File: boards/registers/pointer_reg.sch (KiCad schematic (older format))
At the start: 48 parts, among them U10 74HC161PW, U11 MC74HC244ADT, U12 MC74HC244ADT, U13 74HC161PW, U14 74HC161PW, U15 MC74HC244ADT, U16 MC74HC244ADT, U9 74HC161PW

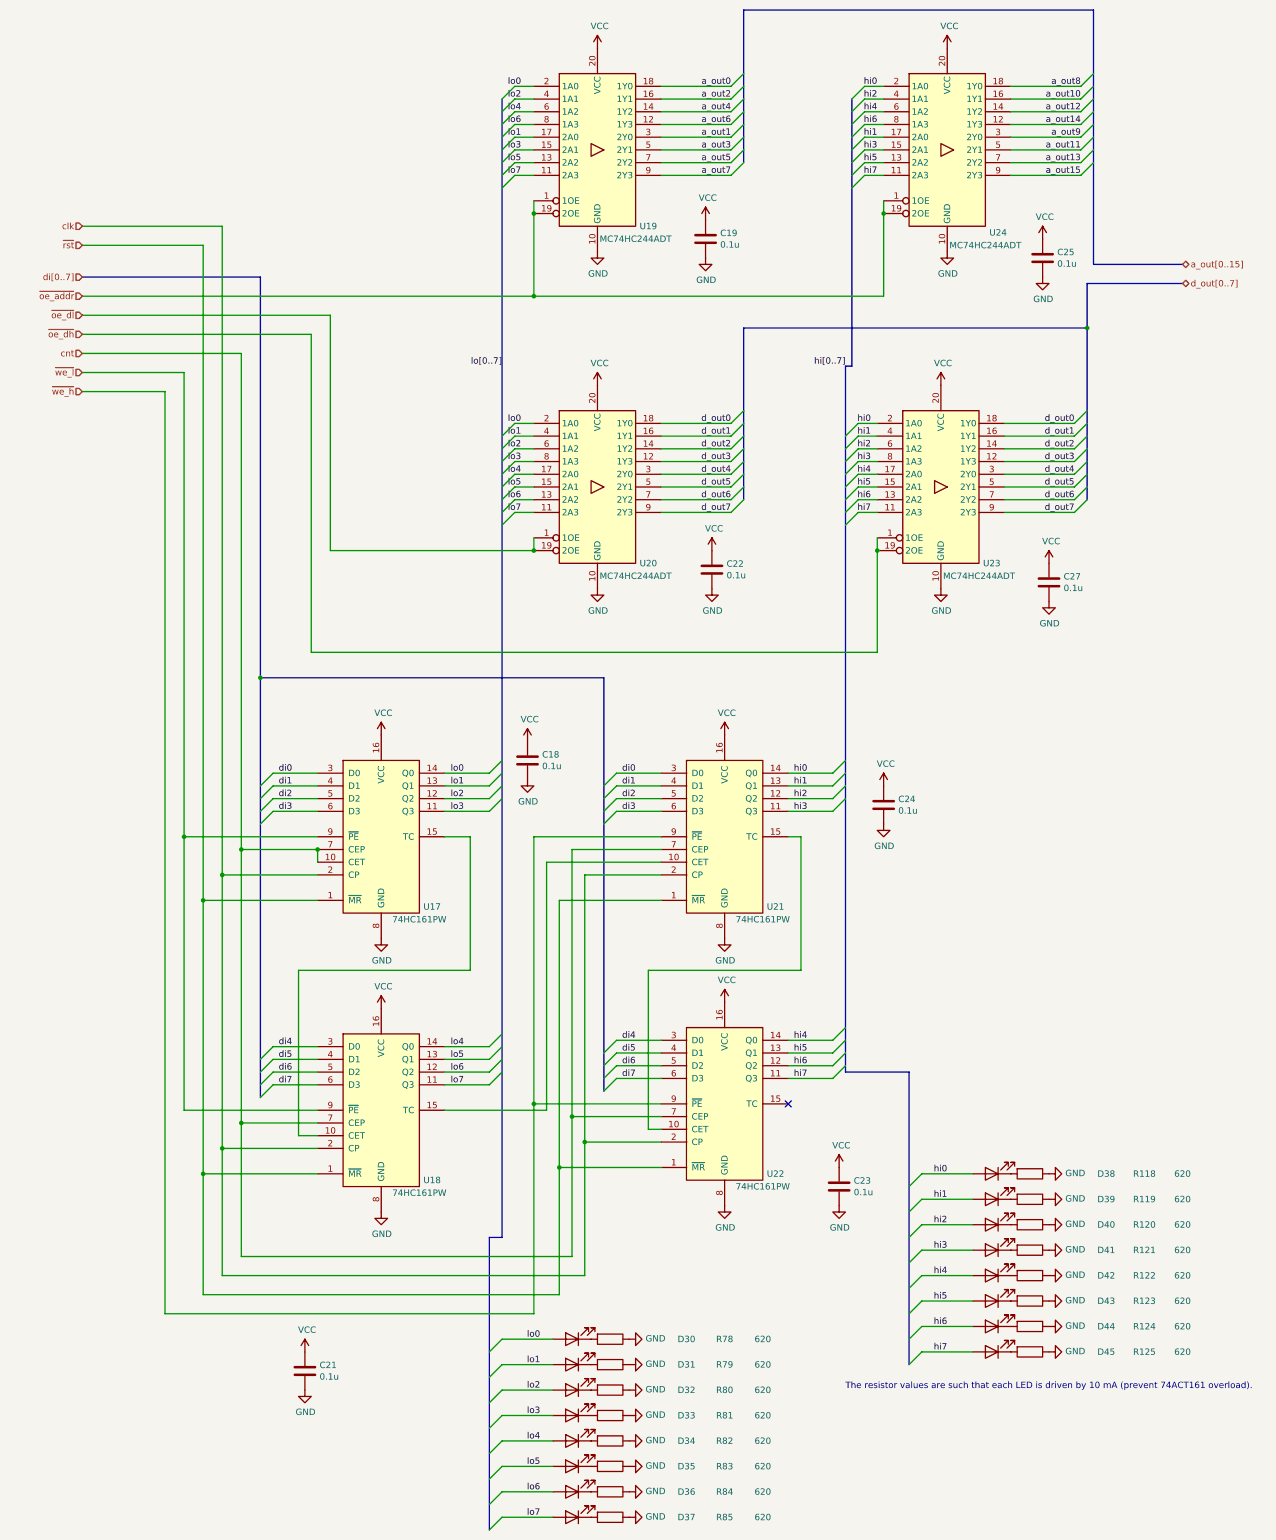
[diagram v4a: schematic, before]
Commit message: Registers board rev. 2
Implement RDY mechanism by suspending clock signal
Take caution against crosstalk on sensitive line
Add proper decoupling capacitors
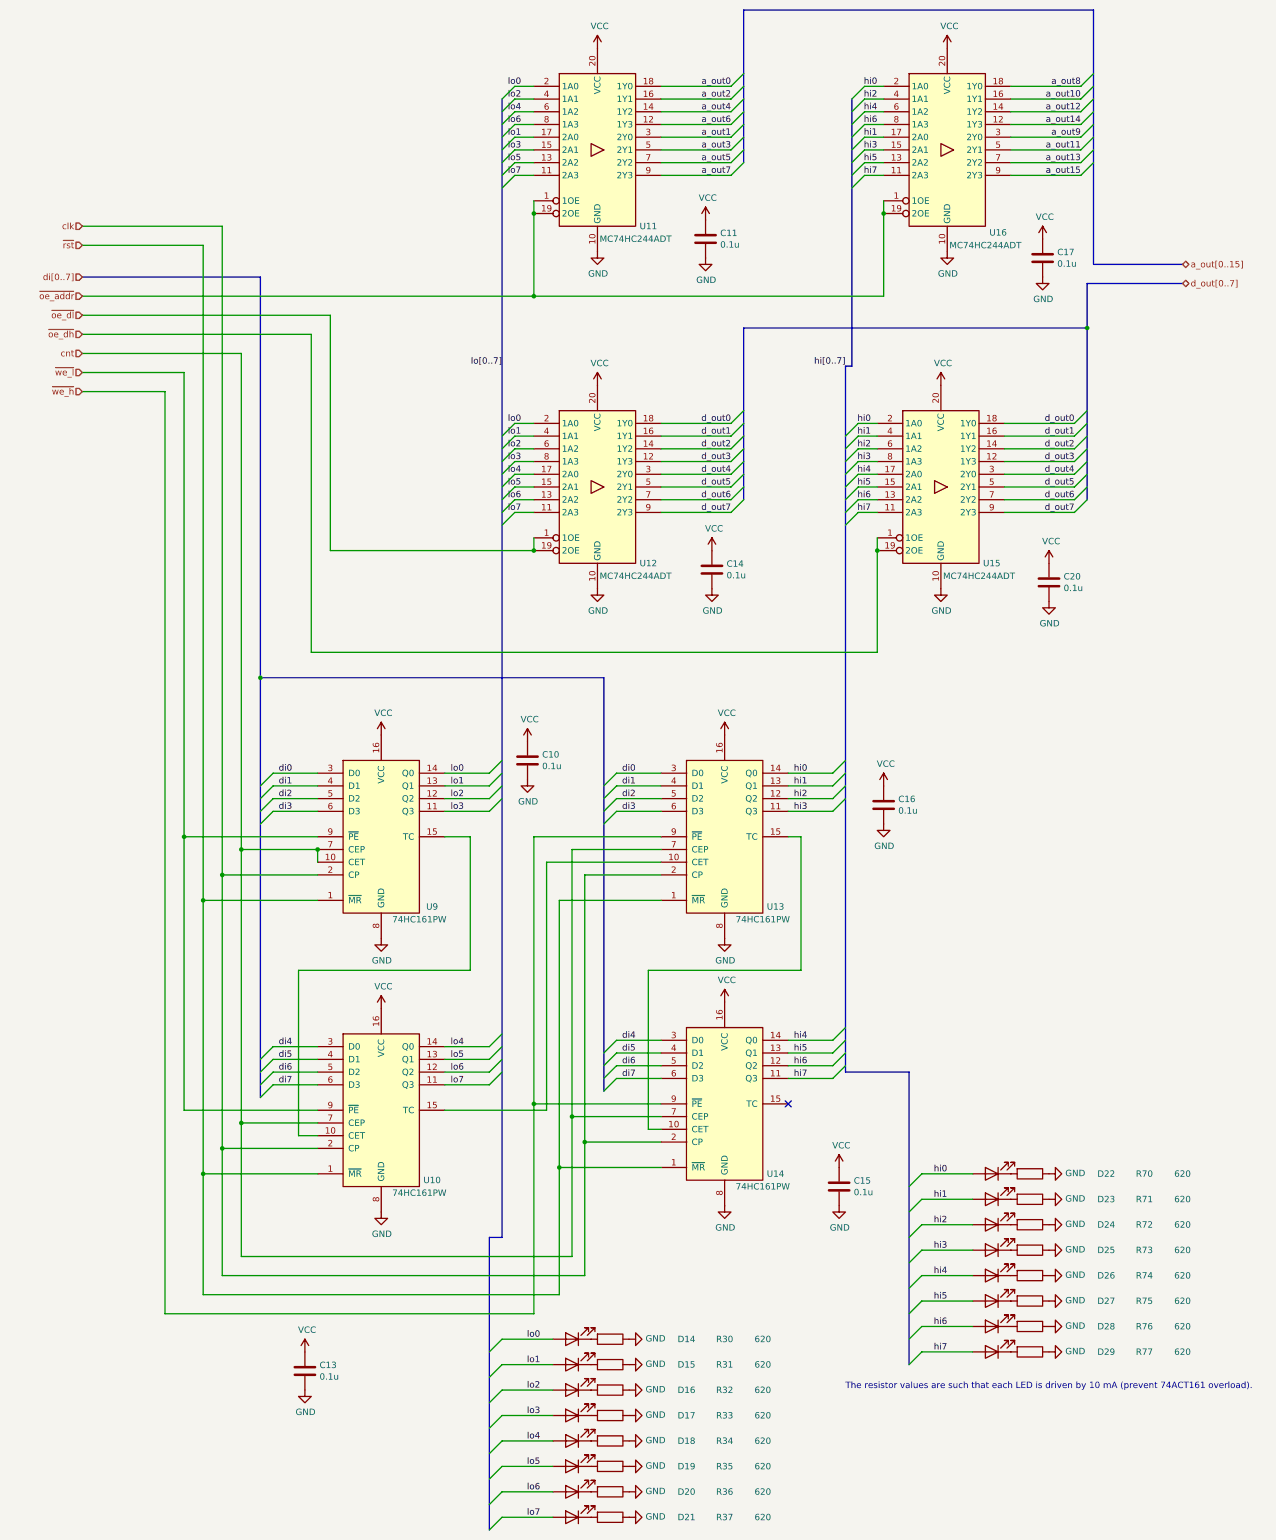
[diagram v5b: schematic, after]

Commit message: Registers: add a pull-up on RDY
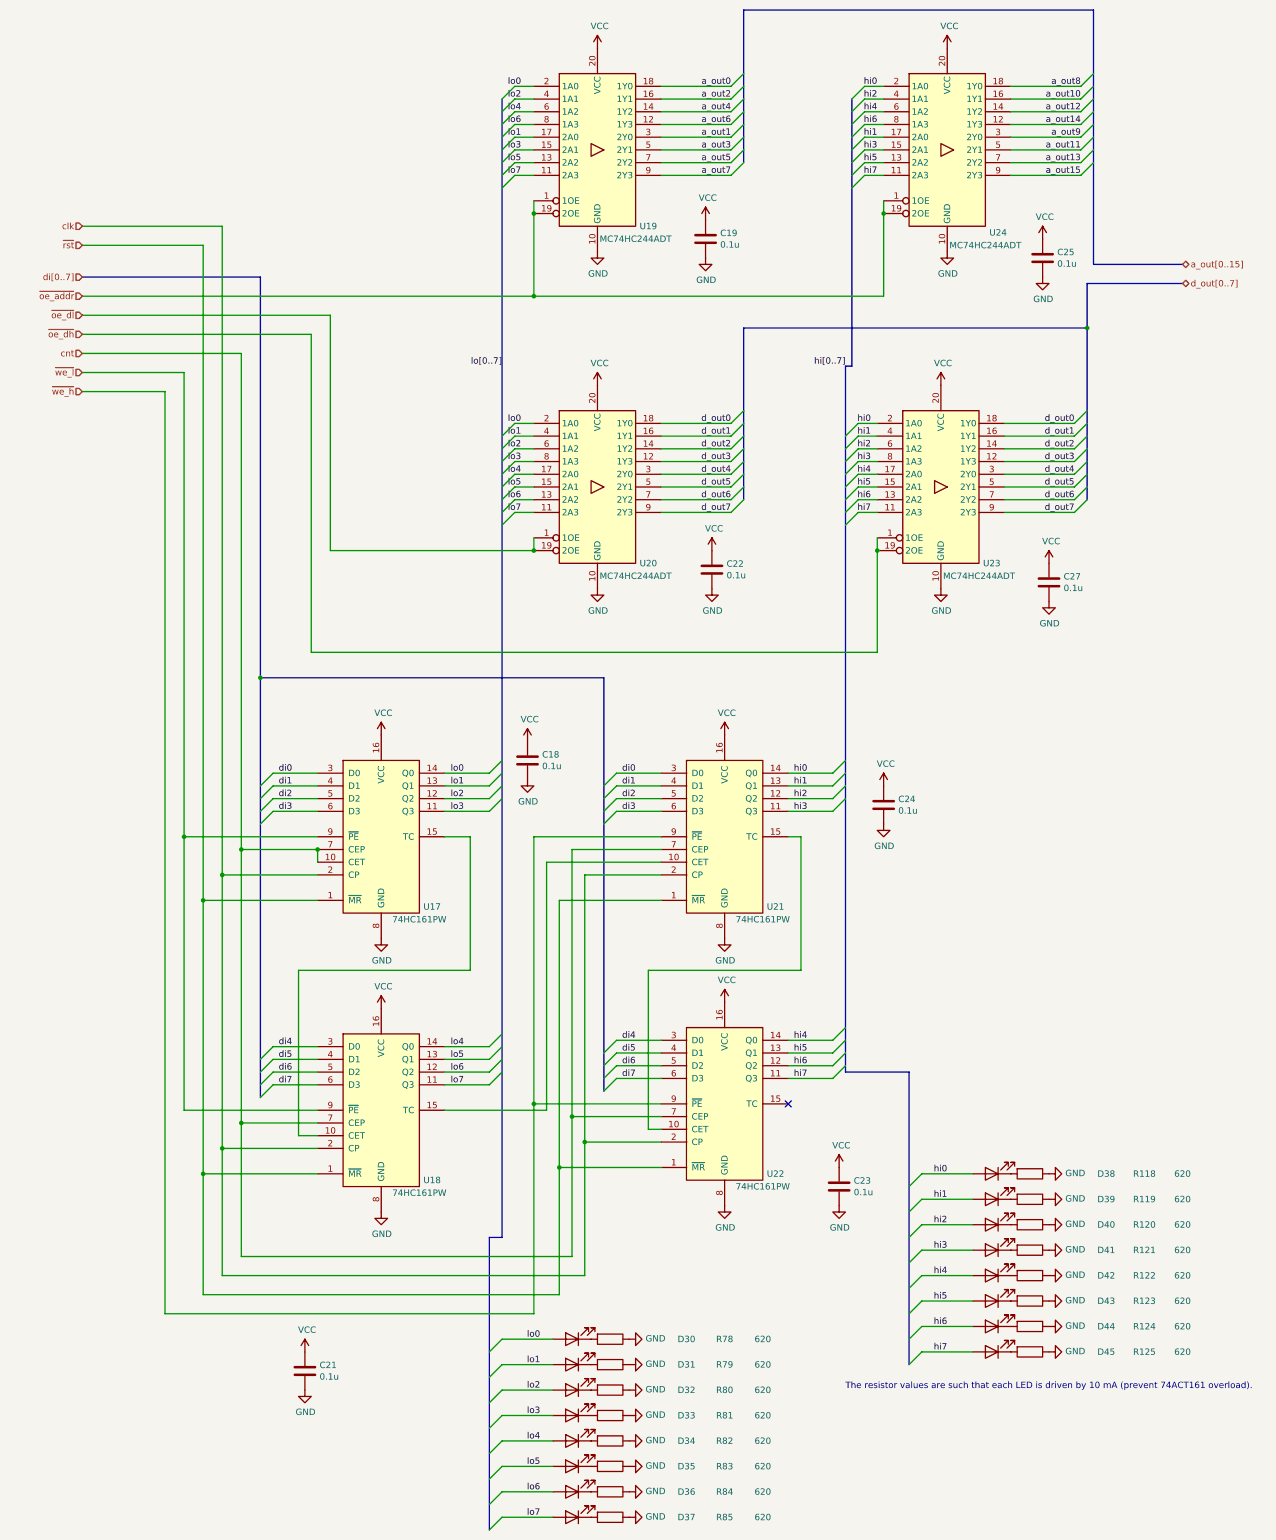
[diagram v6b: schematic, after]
